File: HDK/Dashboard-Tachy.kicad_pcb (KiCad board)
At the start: 2 copper layers, 80 x 80 mm, 54 parts, among them J101 Conn_02x08_Odd_Even, U101 CA56-12CGKWA

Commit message: updated rev1.1
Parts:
- added G***: LOGO, NVF-Kicad:NVF-Logo-30mm, F.Cu at (100.0, 79.4)
- added G***: LOGO, NVF-Kicad:NVF-Logo-30mm, B.Cu at (100.0, 79.4)
- H101, H102, H103, H104: footprint MountingHole:MountingHole_3.2mm_M3_DIN965_Pad_TopBottom -> MountingHole:MountingHole_4.3mm_M4_DIN965_Pad_TopBottom
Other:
- board text added: "JLCJLCJLCJLC"
- board text added: "REV1.1"
- board text added: "Scott CJX, 2024 for NVF2"

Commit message: updated REV1.1
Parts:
- C101, C102, C103, C104, C105, C106, C107, C108, C109, C110, C111, C112, C113, C114, C115, C116, C117, C118, C119, C120, C121, C122, C123, C124: footprint Capacitor_SMD:C_0402_1005Metric -> Capacitor_SMD:C_0603_1608Metric
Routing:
- net GND: track 65.8 -> 73.1 mm
- net +5V: track 67.2 -> 70.3 mm

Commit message: added fab
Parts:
- added kibuzzard-65BA7346: G***, kibuzzard-65BA7346, B.Cu at (99.9, 97.6)
- added kibuzzard-65BA7359: G***, kibuzzard-65BA7359, B.Cu at (102.4, 103.3)
- J101: footprint Connector_JST:JST_PHD_B16B-PHDSS_2x08_P2.00mm_Vertical -> NVF-Kicad:PHD_02x08V-H
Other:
- board text added: "TACHY"

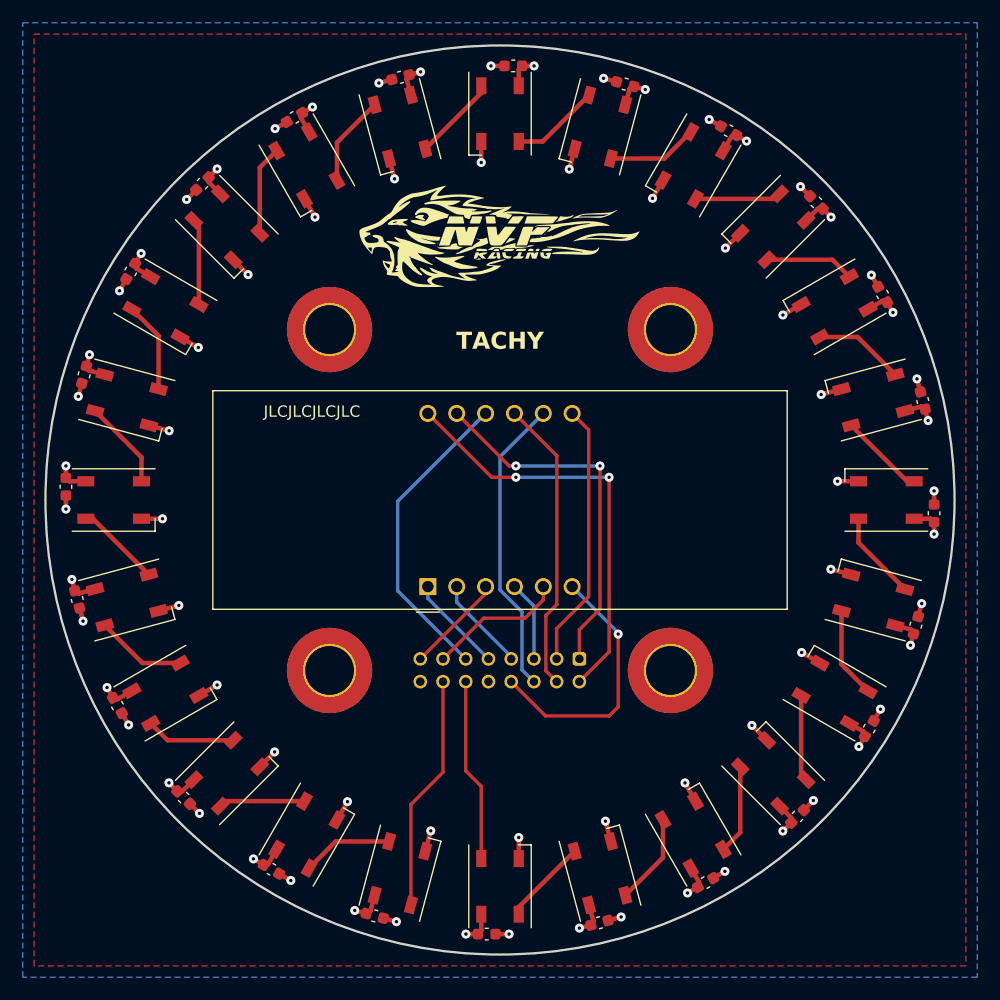
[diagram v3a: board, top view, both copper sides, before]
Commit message: updated dimensions
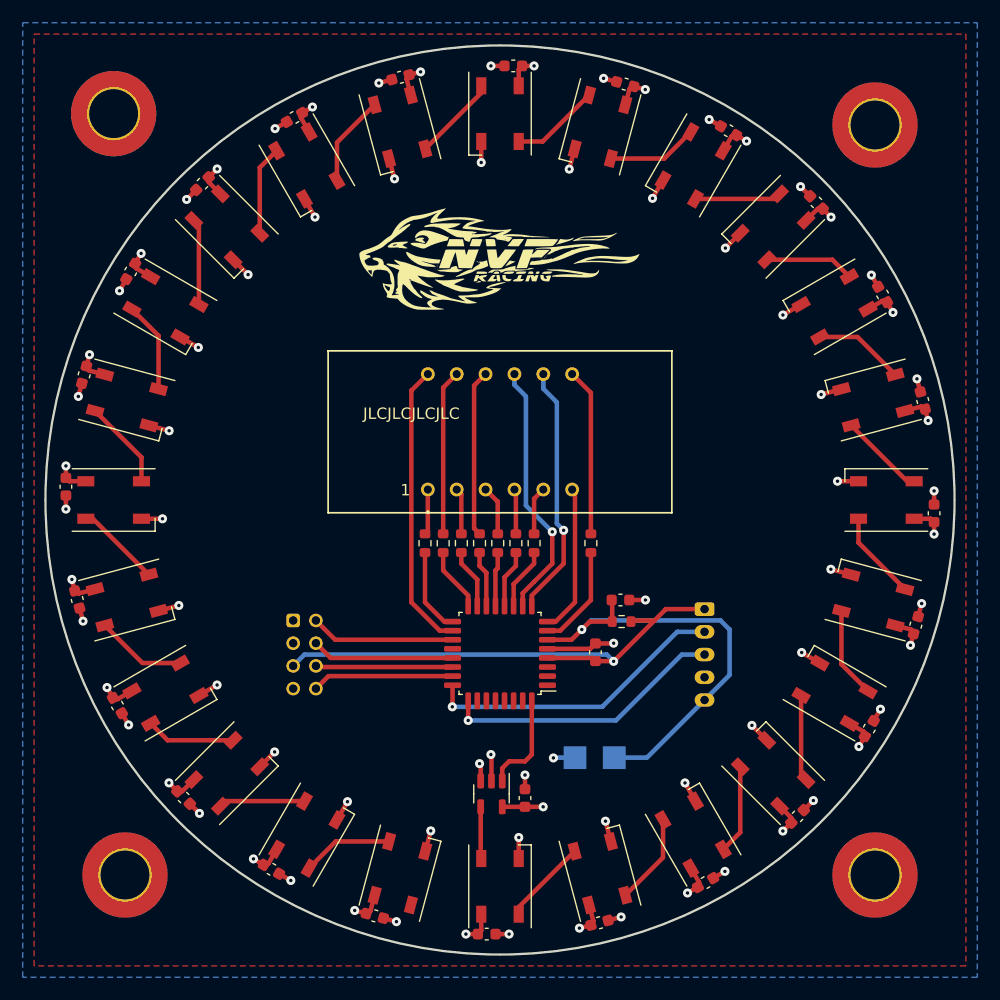
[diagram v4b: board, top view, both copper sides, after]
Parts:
- added C125: 100n, Capacitor_SMD:C_0603_1608Metric, F.Cu at (108.4, 113.4)
- added C126: 100n, Capacitor_SMD:C_0603_1608Metric, F.Cu at (102.2, 126.2)
- added C127: 100n, Capacitor_SMD:C_0603_1608Metric, F.Cu at (110.6, 108.8)
- added R101: 220, Resistor_SMD:R_0603_1608Metric, F.Cu at (95.0, 103.8)
- added R102: 220, Resistor_SMD:R_0603_1608Metric, F.Cu at (108.0, 103.8)
- added R103: 220, Resistor_SMD:R_0603_1608Metric, F.Cu at (101.4, 103.8)
- added R104: 220, Resistor_SMD:R_0603_1608Metric, F.Cu at (96.6, 103.8)
- added R105: 220, Resistor_SMD:R_0603_1608Metric, F.Cu at (93.4, 103.8)
- added R106: 220, Resistor_SMD:R_0603_1608Metric, F.Cu at (98.2, 103.8)
- added R107: 220, Resistor_SMD:R_0603_1608Metric, F.Cu at (103.0, 103.8)
- added R108: 220, Resistor_SMD:R_0603_1608Metric, F.Cu at (99.8, 103.8)
- added R109: 10k, Resistor_SMD:R_0603_1608Metric, F.Cu at (110.7, 110.7)
- added SWD101: SWD_Breakout_Minimal, NVF-Kicad:PH_01x05V-H, B.Cu at (118.0, 113.6)
- added TP101: TestPoint, TestPoint:TestPoint_Pad_2.0x2.0mm, B.Cu at (110.0, 122.7)
- added TP102: TestPoint, TestPoint:TestPoint_Pad_2.0x2.0mm, B.Cu at (106.6, 122.7)
- added U102: STM32G030K6Tx, Package_QFP:LQFP-32_7x7mm_P0.8mm, F.Cu at (100.0, 113.5)
- added U103: 74LVC1G00, Package_TO_SOT_SMD:SOT-23-5, F.Cu at (99.3, 125.9)
- J101: value Conn_02x08_Odd_Even -> Conn_02x04_Odd_Even; footprint NVF-Kicad:PHD_02x08V-H -> NVF-Kicad:PHD_02x04V-H
- U101: footprint Display_7Segment:CA56-12CGKWA -> nvf:LDQ-M3604RI_LUM
- moved H101 26.9 mm to (66.0, 66.0)
- moved H102 25.5 mm to (133.0, 67.0)
- moved H103 25.5 mm to (67.0, 133.0)
- moved H104 25.5 mm to (133.0, 133.0)
- moved kibuzzard-65BA7346 22.2 mm to (122.0, 95.5)
- moved kibuzzard-65BA7359 22.2 mm to (124.5, 101.2)
- moved J101 17.3 mm to (82.8, 113.6), turned to -90 degrees
- moved U101 6.00 mm to (100.0, 94.0), turned to 0 degrees
- moved G*** 2.00 mm to (100.0, 81.4)
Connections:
- J101 pad 1: /7SEG_A -> VCC
- J101 pad 2: /7SEG_CA1 -> /UART_TX
- J101 pad 3: /7SEG_B -> GND
- J101 pad 4: /7SEG_CA2 -> /UART_RX
- J101 pad 5: /7SEG_C -> +3V3
- J101 pad 6: /7SEG_CA3 -> /I2C_SCL
- J101 pad 7: /7SEG_D -> +5V
- J101 pad 8: /7SEG_CA4 -> /I2C_SDA
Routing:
- net +3V3: track 0.00 -> 46.8 mm, vias 0 -> 1
- net /NRST: track 0.00 -> 39.1 mm, vias 0 -> 1
- net /SWDIO: track 0.00 -> 26.8 mm, vias 0 -> 1
- net /SWCLK: track 0.00 -> 24.9 mm, vias 0 -> 1
- net /LED-24-25: track 20.8 -> 0.00 mm
- net /7SEG_A: track 32.3 -> 14.5 mm, vias 2 -> 0
- net /UART_TX: track 0.00 -> 12.7 mm
- net /7SEG_F: track 27.3 -> 14.7 mm
- net /UART_RX: track 0.00 -> 12.6 mm
- net /I2C_SDA: track 0.00 -> 12.5 mm
- net GND: track 73.1 -> 85.3 mm, vias 48 -> 53
- net /I2C_SCL: track 0.00 -> 12.1 mm
- net /7SEG_CA1: track 37.3 -> 25.3 mm, vias 2 -> 0
- net /LED-0-1: track 16.1 -> 4.50 mm
- net /7SEG_CA4: track 23.3 -> 13.2 mm, vias 1 -> 0
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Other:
- board text added: "DB_CON"
- board text added: "NRST"
- board text added: "REV2"
- board text added: "SWD"
- board text removed: "REV1.1"
- board text removed: "TACHY"

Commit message: changed outline
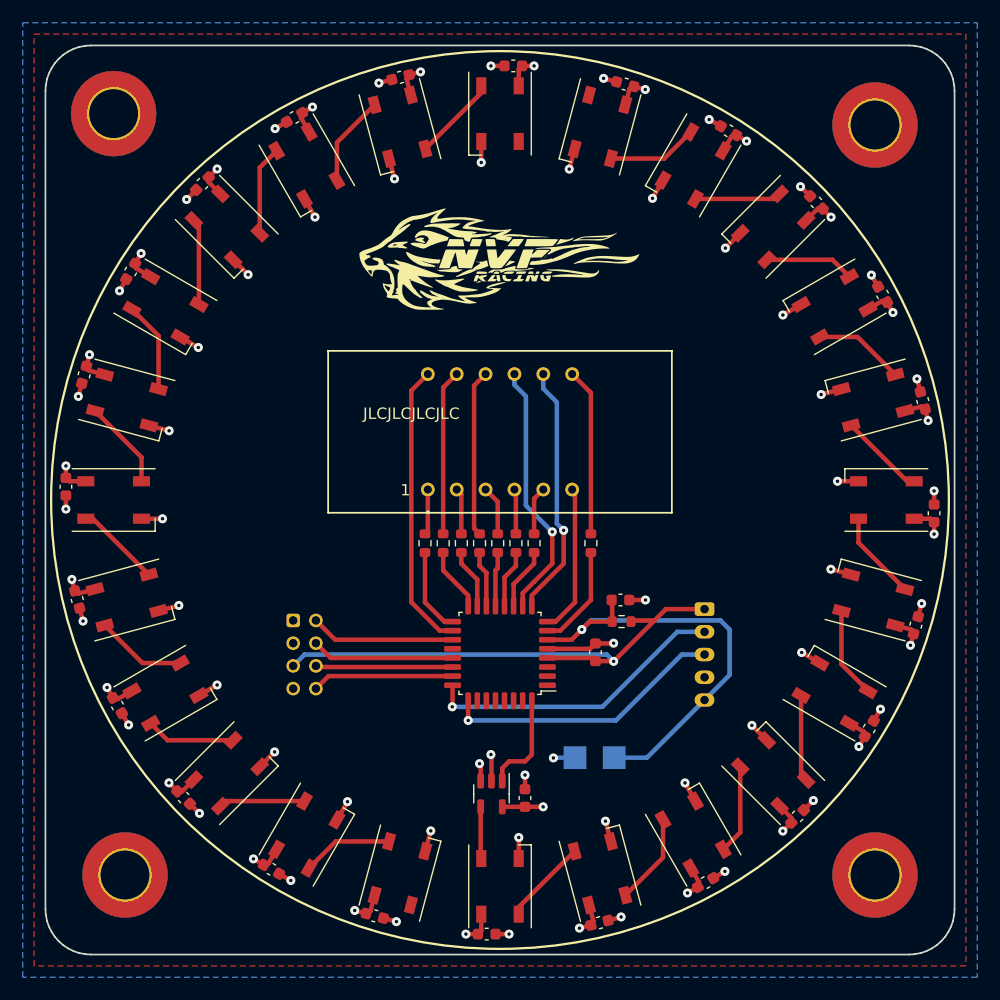
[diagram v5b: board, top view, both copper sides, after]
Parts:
- U101: value CA56-12CGKWA -> LDQ-M3604RI; footprint nvf:LDQ-M3604RI_LUM -> NVF-Kicad:04x7SegmentDispl
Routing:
- net /LED-12-13: track 7.88 -> 0.00 mm
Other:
- outline, holes or cut-outs redrawn
- board text added: "Rev3"
- board text removed: "REV2"
